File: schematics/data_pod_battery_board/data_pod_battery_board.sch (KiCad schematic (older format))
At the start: 38 parts

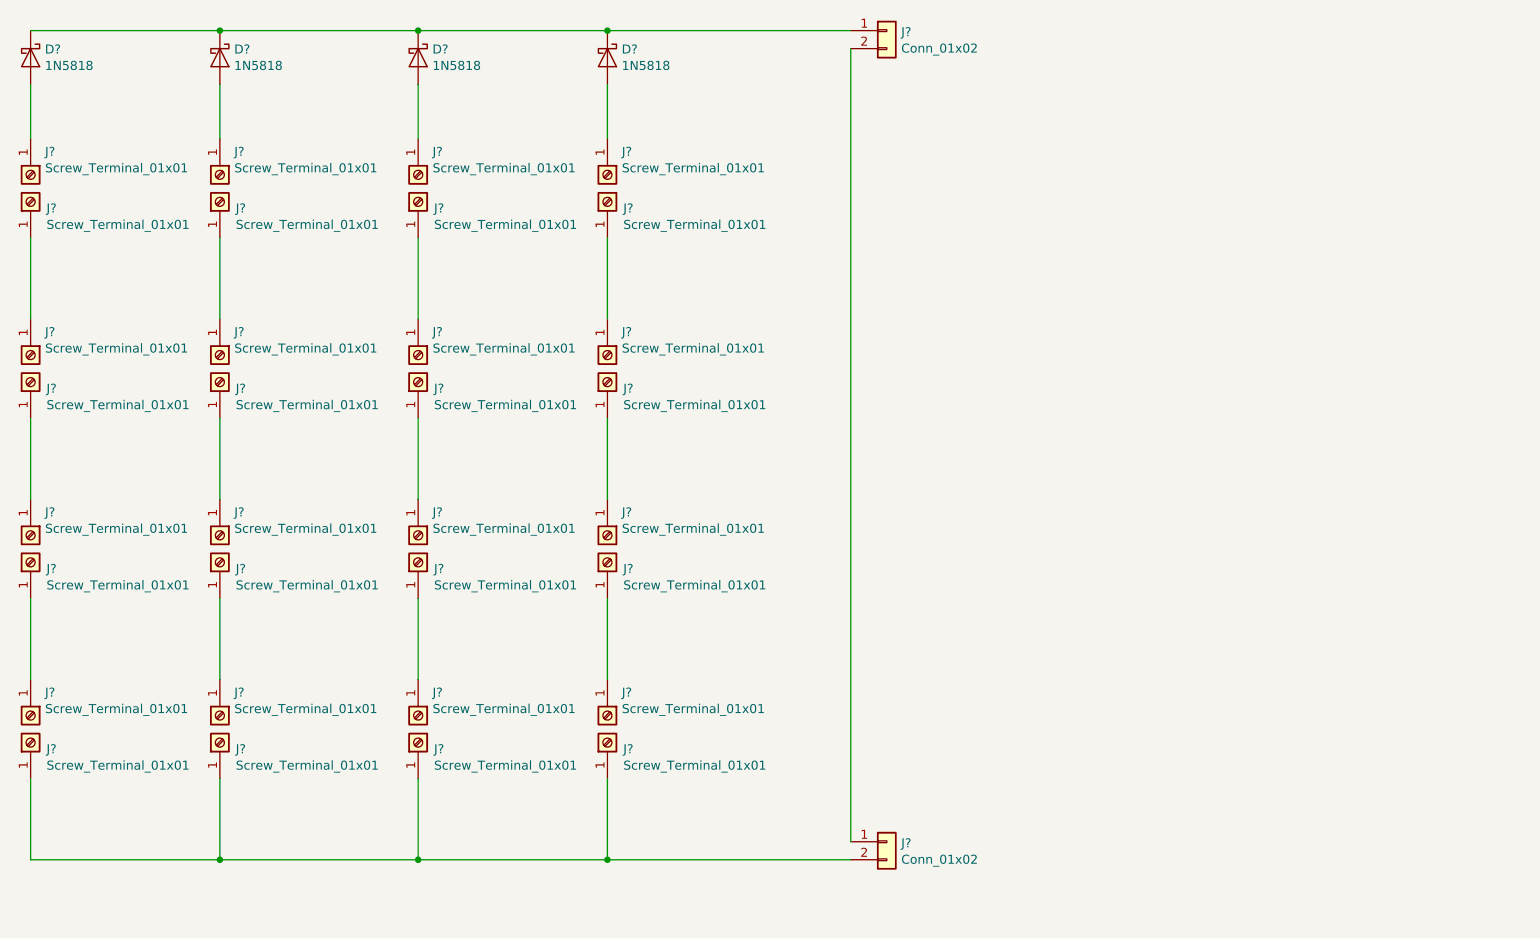
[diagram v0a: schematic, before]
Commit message: created footprint for terminal
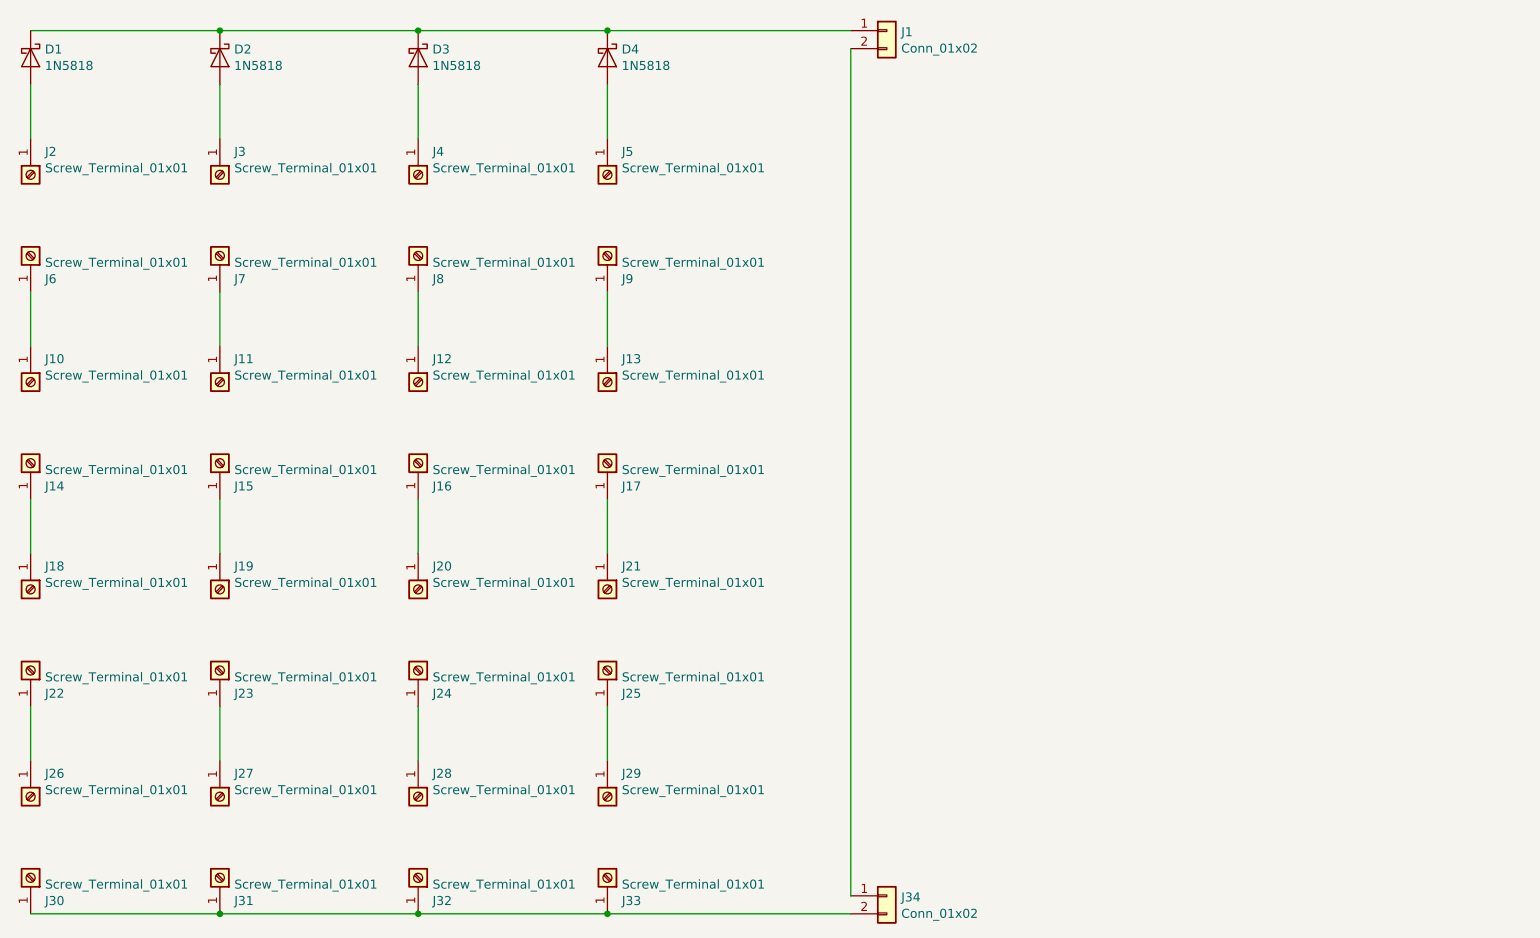
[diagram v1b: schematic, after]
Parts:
- removed J? (x31): Screw_Terminal_01x01, symbol Connector:Screw_Terminal_01x01
- added J10, J11, J12, J13, J14, J15, J16, J17, J18, J19, J20, J21, J22, J23, J24, J25, J26, J27, J28, J29, J3, J30, J31, J32, J33, J4, J5, J6, J7, J8, J9: Screw_Terminal_01x01, terminals:screw_terminal_7.0mmx5.0mm, symbol Connector:Screw_Terminal_01x01
- J2: renamed from J?; footprint (none) -> terminals:screw_terminal_7.0mmx5.0mm
- gave numbers to parts that had none: 6
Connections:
- net at D4.2 (A): now also J5.1 (Pin_1)
- net at D2.2 (A): now also J3.1 (Pin_1)
- net at D3.2 (A): now also J4.1 (Pin_1)
- net at J34.2 (Pin_2): now also J30.1 (Pin_1), J31.1 (Pin_1), J32.1 (Pin_1), J33.1 (Pin_1)
- new net: J10.1 (Pin_1), J6.1 (Pin_1)
- new net: J11.1 (Pin_1), J7.1 (Pin_1)
- new net: J12.1 (Pin_1), J8.1 (Pin_1)
- new net: J13.1 (Pin_1), J9.1 (Pin_1)
- new net: J14.1 (Pin_1), J18.1 (Pin_1)
- new net: J15.1 (Pin_1), J19.1 (Pin_1)
- new net: J16.1 (Pin_1), J20.1 (Pin_1)
- new net: J17.1 (Pin_1), J21.1 (Pin_1)
- new net: J22.1 (Pin_1), J26.1 (Pin_1)
- new net: J23.1 (Pin_1), J27.1 (Pin_1)
- new net: J24.1 (Pin_1), J28.1 (Pin_1)
- new net: J25.1 (Pin_1), J29.1 (Pin_1)
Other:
- moved on the sheet: J34

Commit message: made some more changes to pcb
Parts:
- added D5, D6: 1N5818, Diode_THT:D_DO-41_SOD81_P10.16mm_Horizontal, symbol Diode:1N5818
- added J35, J36, J37, J38, J39, J40, J41, J42, J43, J44, J45, J46, J47, J48, J49, J50: Screw_Terminal_01x01, terminals:screw_terminal_7.0mmx5.0mm, symbol Connector:Screw_Terminal_01x01
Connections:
- net at D1.1 (K), D2.1 (K), D3.1 (K)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: now also D5.1 (K), D6.1 (K)
- net at J30.1 (Pin_1), J31.1 (Pin_1), J32.1 (Pin_1)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: now also J49.1 (Pin_1), J50.1 (Pin_1)
- new net: D6.2 (A), J36.1 (Pin_1)
- new net: D5.2 (A), J35.1 (Pin_1)
- new net: J37.1 (Pin_1), J39.1 (Pin_1)
- new net: J38.1 (Pin_1), J40.1 (Pin_1)
- new net: J41.1 (Pin_1), J43.1 (Pin_1)
- new net: J42.1 (Pin_1), J44.1 (Pin_1)
- new net: J45.1 (Pin_1), J47.1 (Pin_1)
- new net: J46.1 (Pin_1), J48.1 (Pin_1)
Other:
- moved on the sheet: J1, J34

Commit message: added more changes
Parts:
- J1, J34: footprint Connector_Molex:Molex_Mini-Fit_Sr_42819-22XX_1x02_P10.00mm_Vertical -> Connector_Molex:Molex_Nano-Fit_105309-xx02_1x02_P2.50mm_Vertical; Part# WM11908-ND -> WM15036-ND
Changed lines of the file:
@@
 F 0 "J1" H 9730 792 50  0000 L CNN
 F 1 "Conn_01x02" H 9730 701 50  0000 L CNN
-F 2 "Connector_Molex:Molex_Mini-Fit_Sr_42819-22XX_1x02_P10.00mm_Vertical" H 9650 800 50  0001 C CNN
-F 3 "https://www.molex.com/pdm_docs/ps/PS-42815-001.pdf" H 9650 800 50  0001 C CNN
+F 2 "Connector_Molex:Molex_Nano-Fit_105309-xx02_1x02_P2.50mm_Vertical" H 9650 800 50  0001 C CNN
+F 3 "http://www.literature.molex.com/SQLImages/kelmscott/Molex/PDF_Images/987651-1223.PDF" H 9650 800 50  0001 C CNN
 F 4 "Digikey" H 9650 800 50  0001 C CNN "Vendor"
-F 5 "WM11908-ND" H 9650 800 50  0001 C CNN "Part#"
+F 5 "WM15036-ND" H 9650 800 50  0001 C CNN "Part#"
 	1    9650 800
 	1    0    0    -1
@@
 	0    1    1    0
 $EndComp
-$Comp
-L Connector_Generic:Conn_01x02 J34
-U 1 1 5DC9AA9B
-P 9650 5600
-F 0 "J34" H 9730 5592 50  0000 L CNN
-F 1 "Conn_01x02" H 9730 5501 50  0000 L CNN
-F 2 "Connector_Molex:Molex_Mini-Fit_Sr_42819-22XX_1x02_P10.00mm_Vertical" H 9650 5600 50  0001 C CNN
-F 3 "https://www.molex.com/pdm_docs/ps/PS-42815-001.pdf" H 9650 5600 50  0001 C CNN
-F 4 "Digikey" H 9650 5600 50  0001 C CNN "Vendor"
-F 5 "WM11908-ND" H 9650 5600 50  0001 C CNN "Part#"
-	1    9650 5600
-	1    0    0    -1
-$EndComp
 Wire Wire Line
 	1950 2250 1950 2550
@@
 Wire Wire Line
 	9450 900  9450 5600
+$Comp
+L Connector_Generic:Conn_01x02 J34
+U 1 1 5DCCA61A
+P 9650 5600
+F 0 "J34" H 9730 5592 50  0000 L CNN
+F 1 "Conn_01x02" H 9730 5501 50  0000 L CNN
+F 2 "Connector_Molex:Molex_Nano-Fit_105309-xx02_1x02_P2.50mm_Vertical" H 9650 5600 50  0001 C CNN
+F 3 "http://www.literature.molex.com/SQLImages/kelmscott/Molex/PDF_Images/987651-1223.PDF" H 9650 5600 50  0001 C CNN
+F 4 "Digikey" H 9650 5600 50  0001 C CNN "Vendor"
+F 5 "WM15036-ND" H 9650 5600 50  0001 C CNN "Part#"
+	1    9650 5600
+	1    0    0    -1
+$EndComp
 $EndSCHEMATC
